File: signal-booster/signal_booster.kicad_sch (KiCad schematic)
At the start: 13 parts, among them J1 Conn_01x01, J2 Conn_01x01, J3 Conn_01x01, J4 Conn_01x01, J5 Conn_01x01, J6 Conn_01x01, U1 IXDD604PI

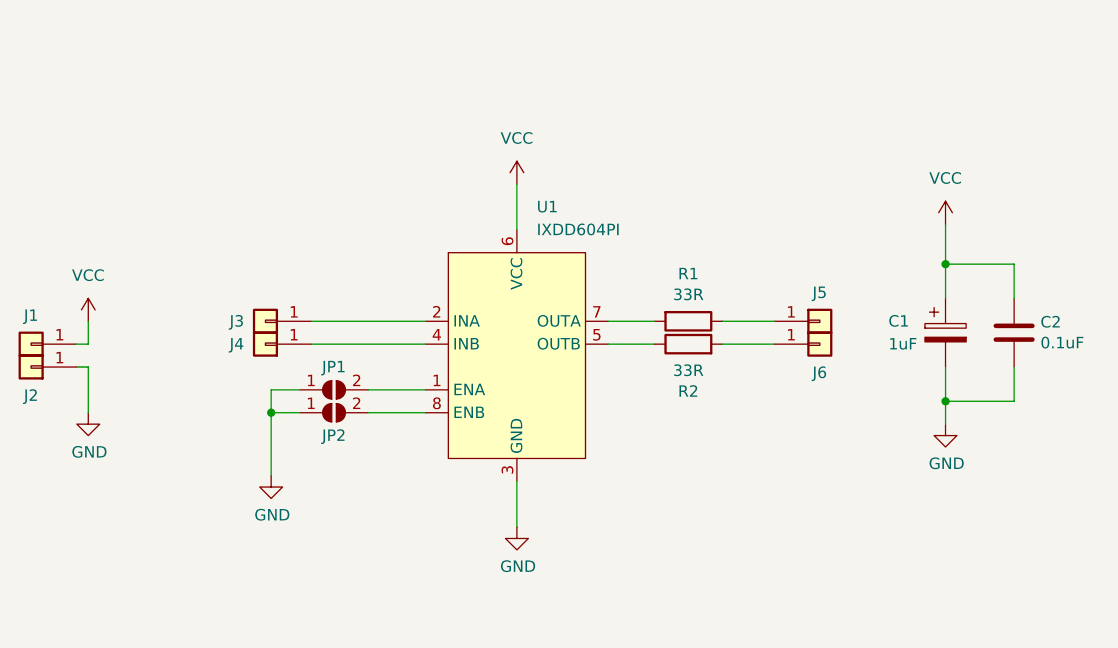
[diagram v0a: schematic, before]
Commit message: Add layout for signal booster
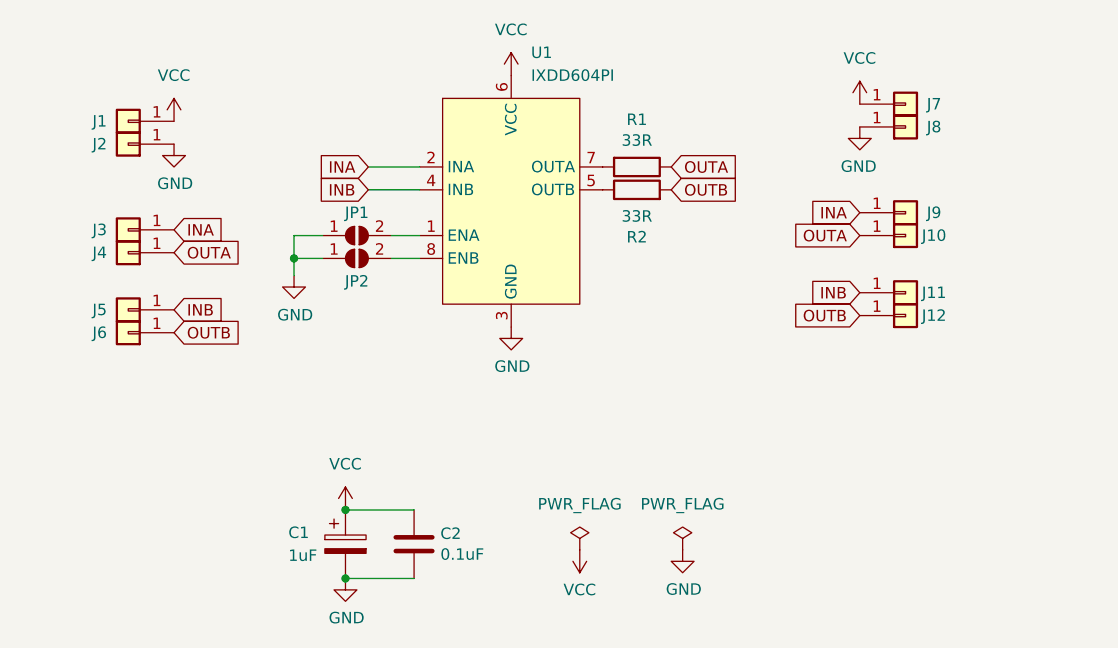
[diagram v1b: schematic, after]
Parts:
- removed J5: Conn_01x01, symbol Connector_Generic:Conn_01x01
- added J10, J11, J12, J4, J7, J8, J9: Conn_01x01, Connector_Wire:SolderWire-0.5sqmm_1x01_D0.9mm_OD2.1mm, symbol Connector_Generic:Conn_01x01
- C1: footprint (none) -> Capacitor_THT:CP_Radial_D4.0mm_P2.00mm
- J1, J2, J3, J6: footprint (none) -> Connector_Wire:SolderWire-0.5sqmm_1x01_D0.9mm_OD2.1mm
- J5: renamed from J4; footprint (none) -> Connector_Wire:SolderWire-0.5sqmm_1x01_D0.9mm_OD2.1mm
- JP1, JP2: footprint (none) -> Jumper:SolderJumper-2_P1.3mm_Open_RoundedPad1.0x1.5mm
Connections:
- net GND: now also J8.1 (Pin_1)
- net VCC: now also J7.1 (Pin_1)
- net INA: now reaches J3.1 (Pin_1), U1.2 (INA)
- net INA: now also J9.1 (Pin_1)
- net INB: now reaches J5.1 (Pin_1), U1.4 (INB)
- net INB: now also J11.1 (Pin_1)
- net OUTA: now reaches R1.1
- net OUTA: now also J10.1 (Pin_1), J4.1 (Pin_1)
- net OUTB: now reaches J6.1 (Pin_1), R2.2
- net OUTB: now also J12.1 (Pin_1)
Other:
- moved on the sheet: C1, C2, J1, J2, J3, J5, JP1, JP2, R1, R2, U1
